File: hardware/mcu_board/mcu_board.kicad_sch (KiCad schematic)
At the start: 4 parts, among them J1 Light, J2 Conn_ESP32-H2_Super-Mini_-_Pi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, J3 Touch, J4 Input

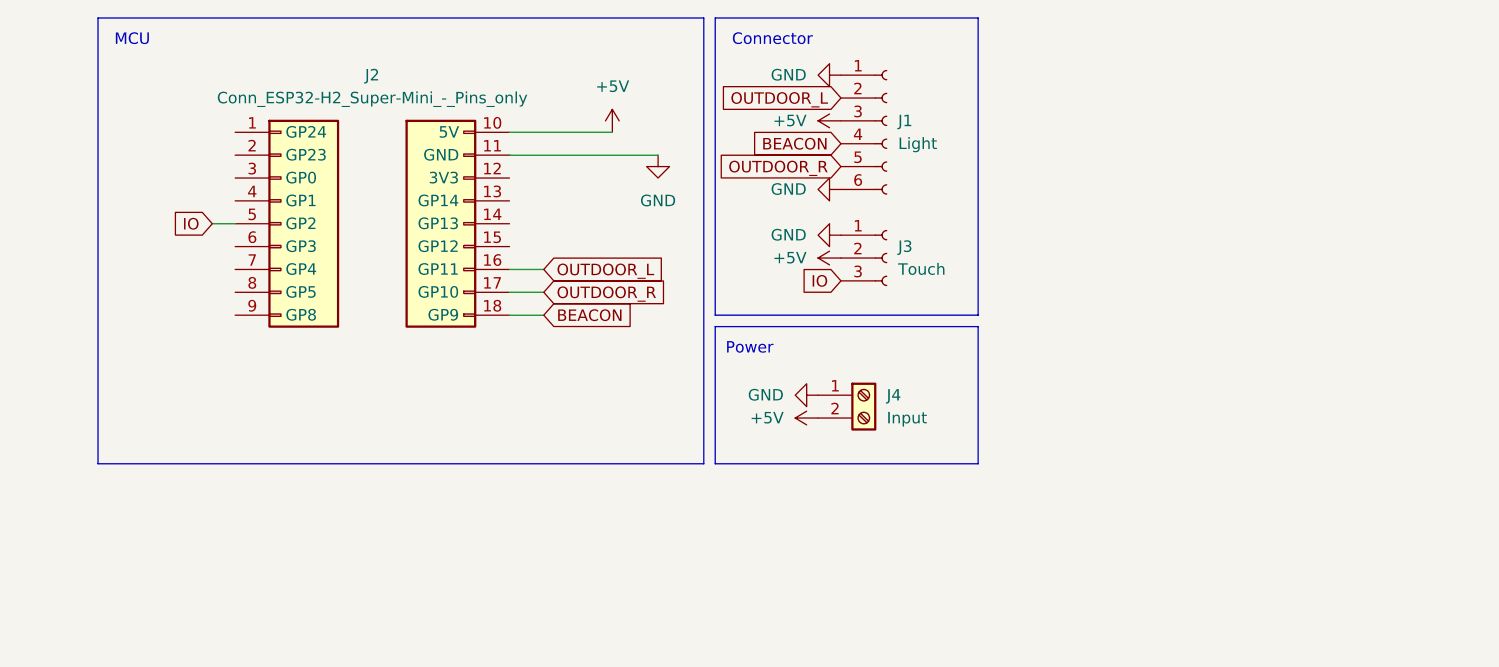
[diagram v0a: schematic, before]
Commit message: latest mcu_board revision
added buck converter

Signed-off-by: Peter Siegmund <mars3142@users.noreply.github.com>
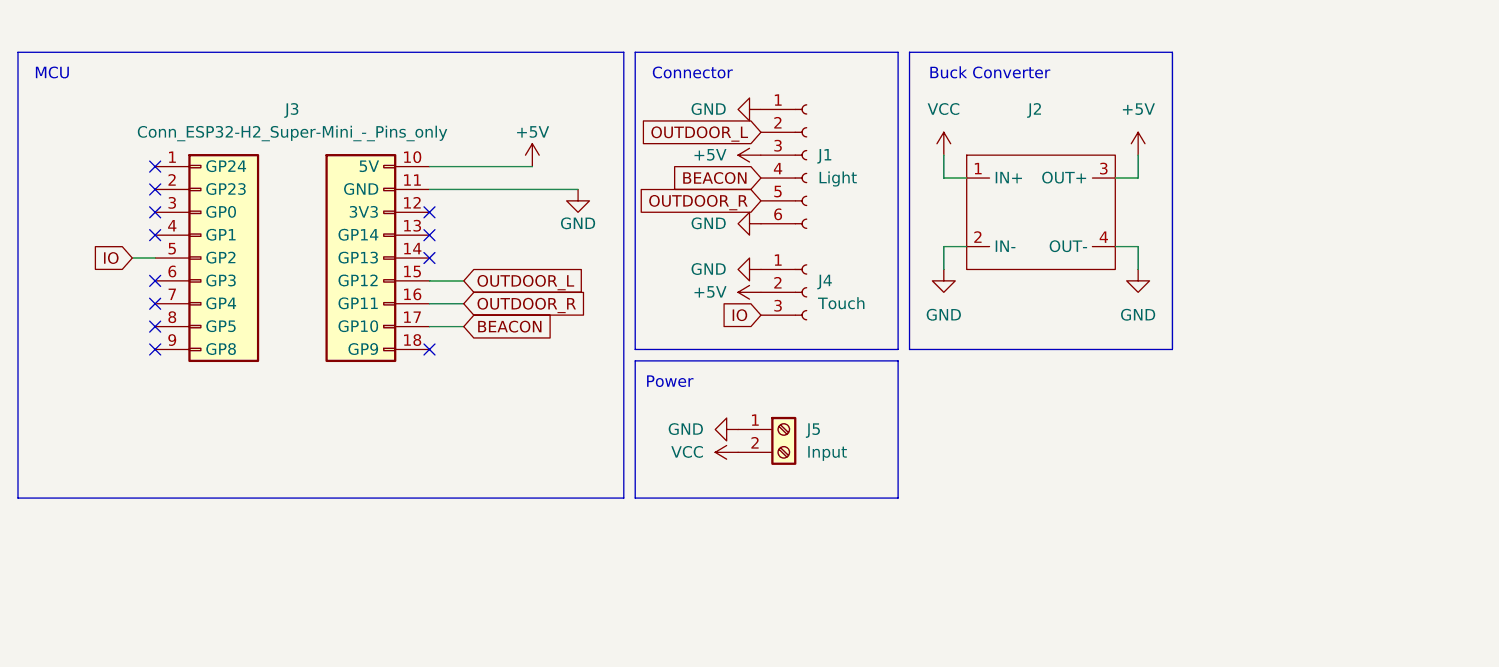
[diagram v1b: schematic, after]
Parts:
- added J2: ~, aliexpress:Buck Converter (30V to 5V), symbol aliexpress:Buck_Converter
- renumbered J2 to J3, J3 to J4, J4 to J5
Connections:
- net +5V: now also J2.3 (OUT+); no longer J5.2 (Pin_2)
- net BEACON: now also J3.17 (GP10); no longer J3.18 (GP9)
- net GND: now also J2.2 (IN-), J2.4 (OUT-)
- net OUTDOOR_L: now also J3.15 (GP12); no longer J3.16 (GP11)
- net OUTDOOR_R: now also J3.16 (GP11); no longer J3.17 (GP10)
- new net VCC: J2.1 (IN+), J5.2 (Pin_2)
- no-connect marks 0 -> 12
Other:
- note added: "Buck Converter"
- moved on the sheet: J1, J3, J4, J5

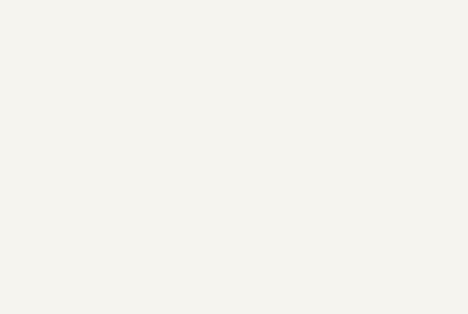
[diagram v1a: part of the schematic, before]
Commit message: add sponsor to PCBs
Signed-off-by: Peter Siegmund <mars3142@users.noreply.github.com>
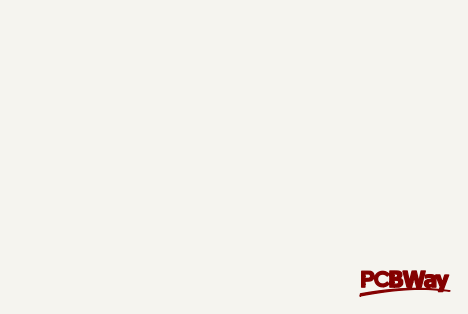
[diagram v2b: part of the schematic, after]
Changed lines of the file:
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@@
+	)
+	(symbol
+		(lib_id "pcbway:LOGO")
+		(at 191.77 106.68 0)
+		(unit 1)
+		(exclude_from_sim no)
+		(in_bom yes)
+		(on_board yes)
+		(dnp no)
+		(fields_autoplaced yes)
+		(property "Reference" "#G1"
+			(at 191.77 105.2885 0)
+			(effects
+				(font
+					(size 1.27 1.27)
+				)
+				(hide yes)
+			)
+		)
+		(property "Value" "LOGO"
+			(at 191.77 108.0715 0)
+			(effects
+				(font
+					(size 1.27 1.27)
+				)
+				(hide yes)
+			)
+		)
+		(property "Footprint" ""
+			(at 191.77 106.68 0)
+			(effects
+				(font
+					(size 1.27 1.27)
+				)
+				(hide yes)
+			)
+		)
+		(property "Datasheet" ""
+			(at 191.77 106.68 0)
+			(effects
+				(font
+					(size 1.27 1.27)
+				)
+				(hide yes)
+			)
+		)
+		(property "Description" ""
+			(at 191.77 106.68 0)
+			(effects
+				(font
+					(size 1.27 1.27)
+				)
+				(hide yes)
+			)
+		)
+		(instances
+			(project ""
+				(path "/7f117d42-0d8b-4a32-a9d3-0b04c0222a5a"
+					(reference "#G1")
+					(unit 1)
+				)
+			)
+		)
 	)
 	(symbol

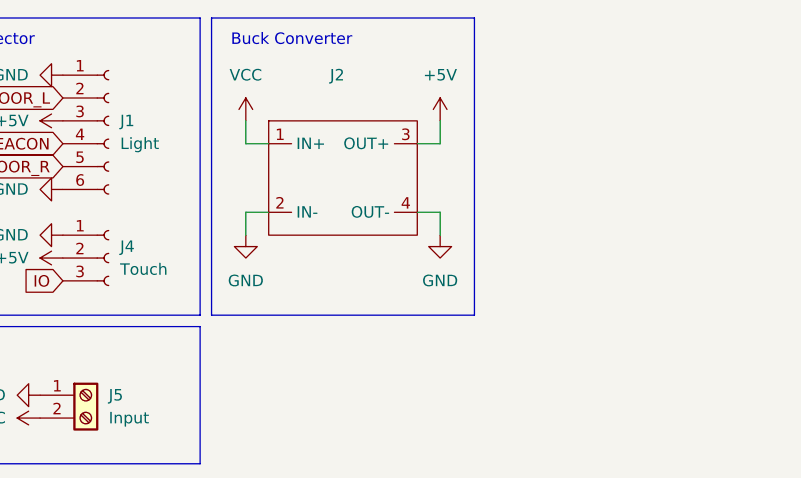
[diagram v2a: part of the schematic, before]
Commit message: new mcu board design
Signed-off-by: Peter Siegmund <mars3142@users.noreply.github.com>
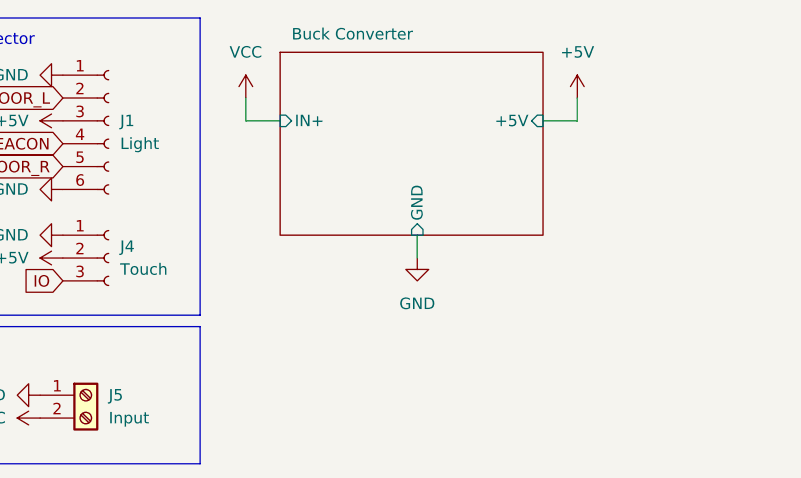
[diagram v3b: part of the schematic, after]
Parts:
- removed J2: ~, aliexpress:Buck Converter (30V to 5V), symbol aliexpress:Buck_Converter
- J1: footprint Connector_JST:JST_PH_S4B-PH-K_1x06_P2.00mm_Horizontal -> Connector_JST:JST_PH_S6B-PH-K_1x06_P2.00mm_Horizontal
- J3: footprint wemos:PinSocket_S3 Zero -> wemos:PinSocket_H2 Super-Mini
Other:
- added sheet Buck Converter (buck_converter.kicad_sch)
- note removed: "Buck Converter"
